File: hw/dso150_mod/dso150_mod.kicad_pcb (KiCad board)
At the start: 4 copper layers, 20.8 x 49.8 mm, 23 parts, among them J1 USB_C_Receptacle_USB2.0, J2 Conn_01x02, J3 Conn_01x02, J4 Conn_01x04, J5 Conn_01x02, J6 Conn_01x01, SW1 SW_SPDT, U1 AP3012, U2 MCP73832-2-OT

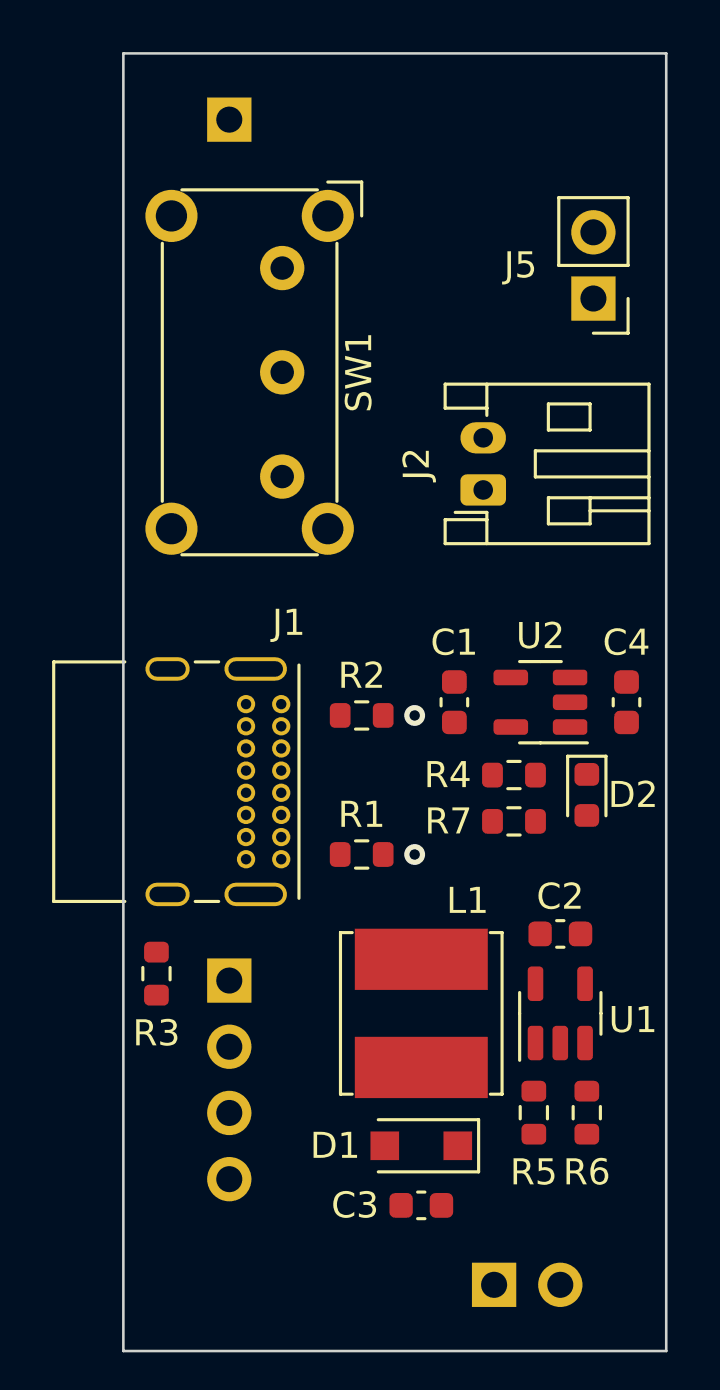
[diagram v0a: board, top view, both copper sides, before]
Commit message: More layout placement, start traces
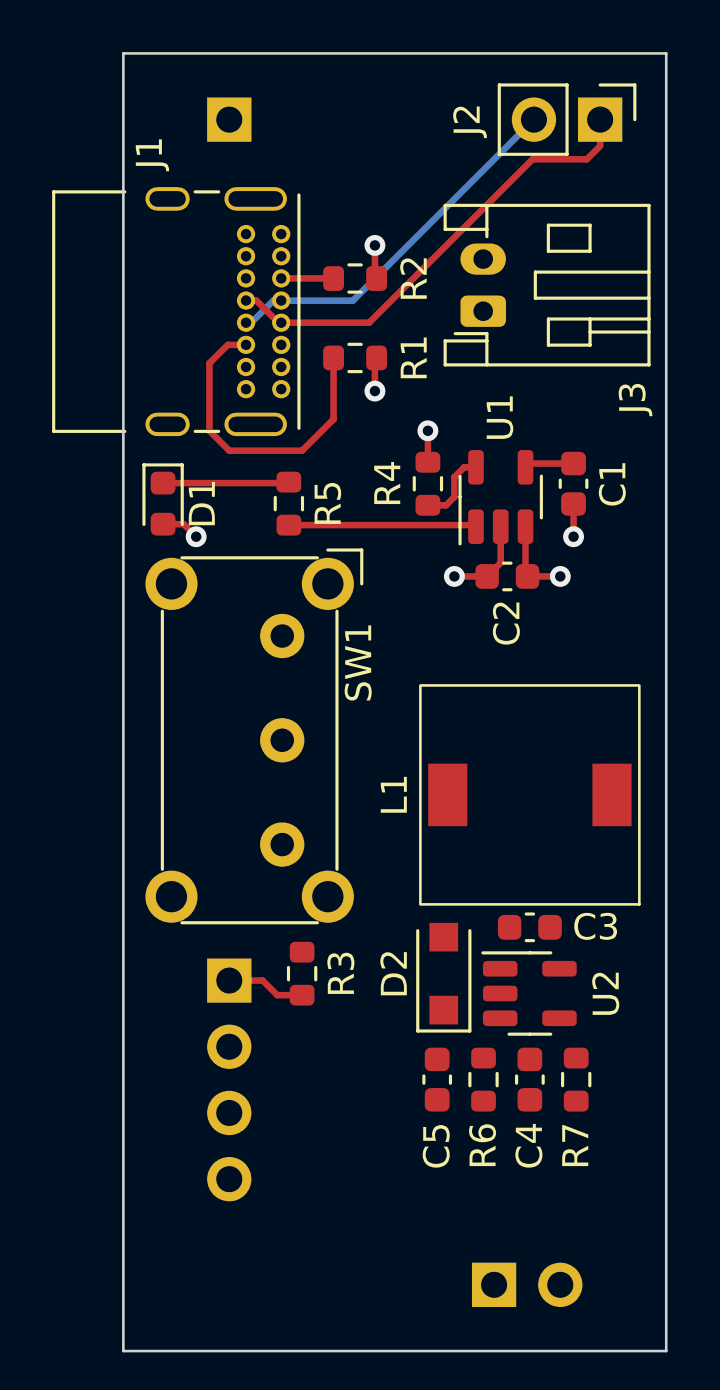
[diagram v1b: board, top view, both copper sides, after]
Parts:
- removed the D1 at (118.6, 124.2)
- removed the U1 at (124.0, 119.1)
- added C4: 4.7p, Capacitor_SMD:C_0603_1608Metric, F.Cu at (122.8, 121.7)
- added D2: MBR1020VL, Diode_SMD:D_SOD-123F, F.Cu at (119.5, 117.6)
- added U2: LMR62014XMF, Package_TO_SOT_SMD:SOT-23-5, F.Cu at (122.8, 118.4)
- C3: renamed from C2; value 1u -> 2.2u
- C5: renamed from C3; value 1u -> 10u
- L1: value 10u -> 12u; footprint Inductor_SMD:L_Bourns_SRN6045TA -> dso150_mod:L_Bourns_SRR0745A
- R6: renamed from R5; value R -> 86.6k
- R7: renamed from R6; value R -> 13.3k
- moved D1 19.7 mm to (108.7, 99.6)
- moved R1 19.1 mm to (116.1, 94.0)
- moved J1 18.0 mm to (113.2, 89.2)
- moved R2 16.8 mm to (116.1, 90.9)
- moved R5 14.9 mm to (113.5, 99.6), turned to 90 degrees
- moved SW1 14.1 mm to (113.3, 104.6)
- moved R4 11.7 mm to (118.9, 98.8), turned to 90 degrees
- moved C1 9.55 mm to (124.5, 98.8)
- moved L1 9.36 mm to (122.8, 110.7), turned to 180 degrees
- moved U1 8.02 mm to (121.7, 99.3), turned to 90 degrees
- moved J2 6.87 mm to (125.5, 84.8), turned to -90 degrees
- moved J3 6.86 mm to (121.0, 92.2)
- moved C2 6.65 mm to (121.9, 102.4), turned to 180 degrees
- moved R3 5.59 mm to (114.0, 117.6)
- moved C5 4.86 mm to (119.2, 121.7), turned to 90 degrees
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- renumbered C4 to C2, D2 to D1, J5 to J2, J2 to J3, J3 to J4, J4 to J5, R7 to R5, U2 to U1
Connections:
- D1 pad 1: Net-(D2-Pad1) -> Net-(R5-Pad2)
- D1 pad 2: Net-(D2-Pad2) (its old number) -> +5V
- J4 pad 1: +9V -> Net-(J4-Pad1)
- R5 pad 1: Net-(D2-Pad2) (its old number) -> Net-(U1-Pad1)
- R5 pad 2: +5V -> Net-(R5-Pad2)
- SW1 pad 1: unconnected-(SW1-Pad1) -> Net-(J4-Pad1)
- SW1 pad 2: unconnected-(SW1-Pad2) -> +9V
- U1 pad 1: Net-(D2-Pad1) -> Net-(U1-Pad1)
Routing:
- net Net-(J1-PadA7): track 0.00 -> 17.8 mm
- net Net-(J1-PadA6): track 0.00 -> 14.3 mm
- net Net-(J1-PadB5): track 0.00 -> 12.2 mm
- net GND: track 0.00 -> 8.44 mm, vias 2 -> 5
- net Net-(U1-Pad1): track 0.00 -> 7.20 mm
- net Net-(R5-Pad2): track 0.00 -> 4.84 mm
- net +5V: track 0.00 -> 3.37 mm, vias 0 -> 1
- net +BATT: track 0.00 -> 3.20 mm, vias 0 -> 1
- net +3.3V: track 0.00 -> 3.03 mm
- net Net-(R4-Pad1): track 0.00 -> 2.89 mm
- net Net-(J1-PadA5): track 0.00 -> 2.01 mm
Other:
- board text added: "JLCJLCJLCJLC"

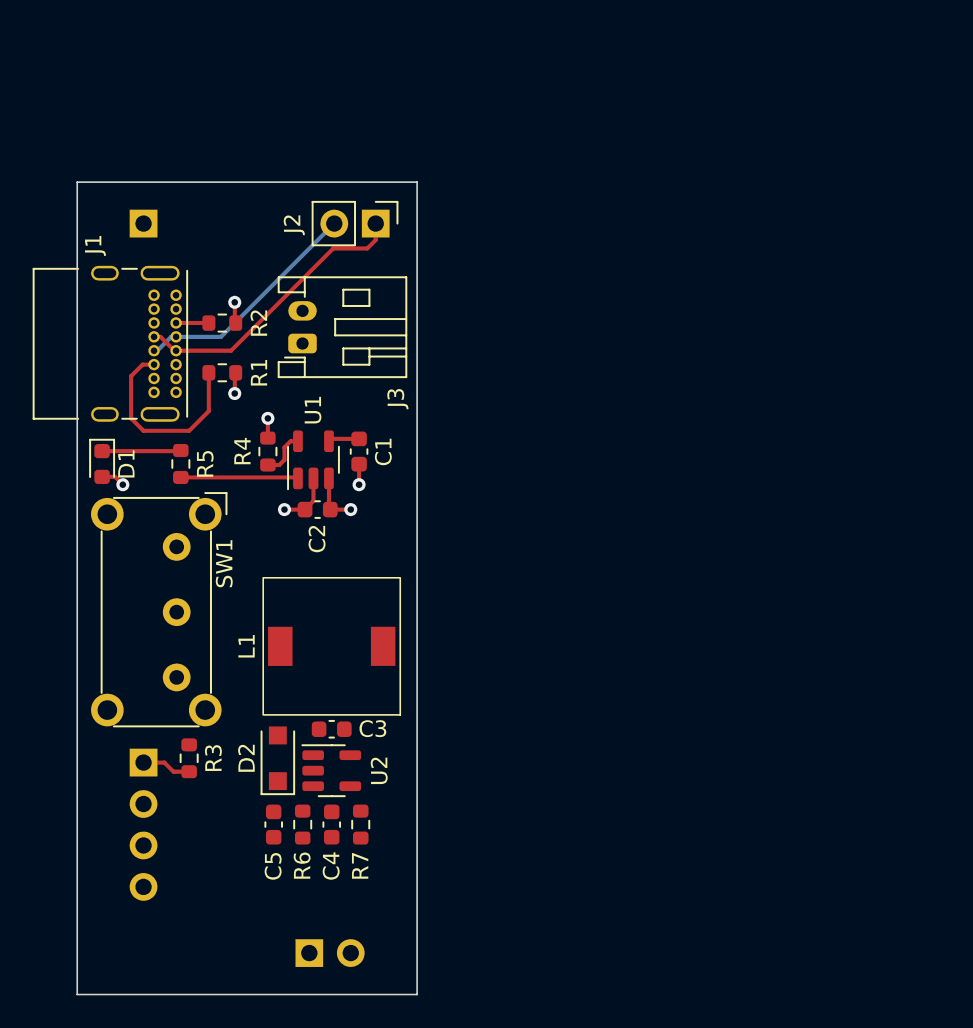
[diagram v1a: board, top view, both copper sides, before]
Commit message: Disable boost converter to conserve battery, first final layout complete
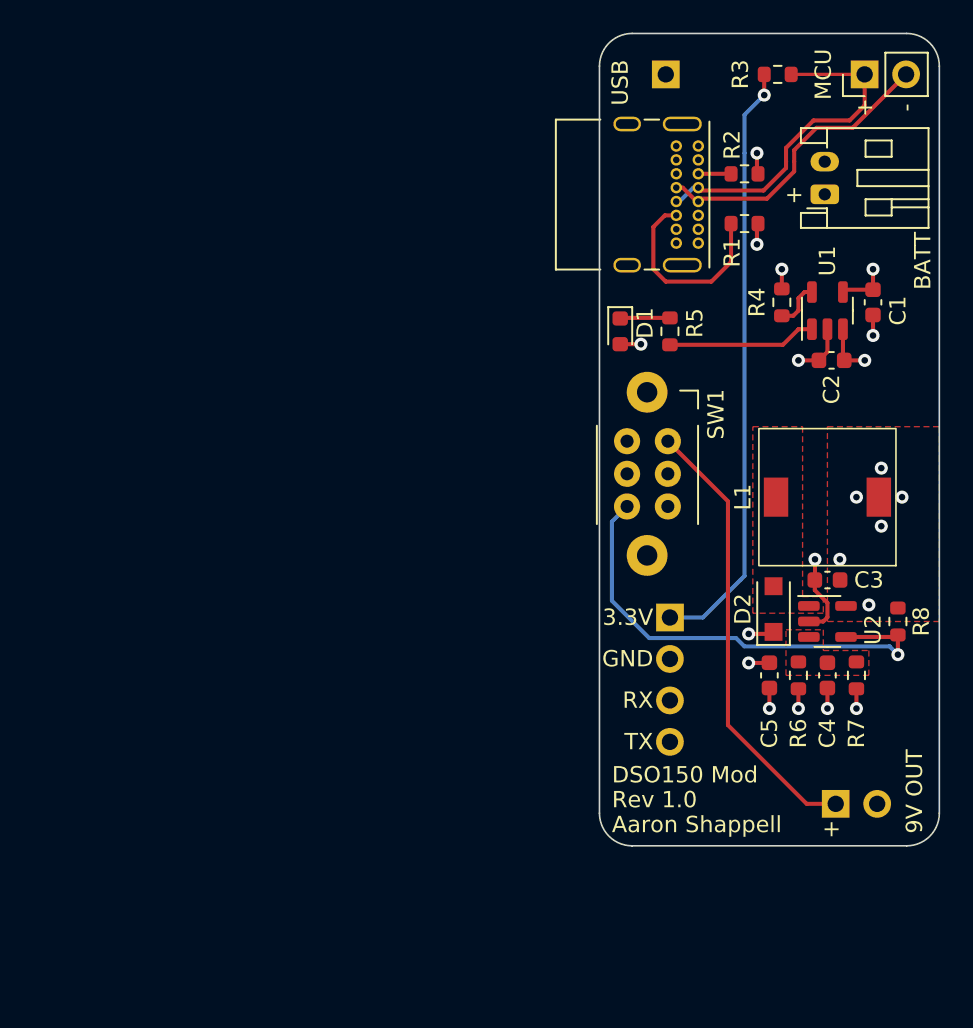
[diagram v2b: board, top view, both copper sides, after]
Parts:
- added R8: 50k, Resistor_SMD:R_0603_1608Metric, F.Cu at (157.5, 109.2)
- J1: footprint Connector_USB:USB_C_Receptacle_GCT_USB4085 -> dso150_mod:USB_C_Receptacle_GCT_USB4085
- SW1: value SW_SPDT -> EG2208; footprint Button_Switch_THT:SW_E-Switch_EG1224_SPDT_Angled -> dso150_mod:SW_E-Switch_EG2208_DPDT_Angled
- moved R3 55.3 mm to (150.1, 75.7), turned to 0 degrees
- moved J4 33.5 mm to (153.7, 120.4)
- moved J5 33.5 mm to (143.5, 109.0)
- moved J6 33.3 mm to (143.3, 75.7)
- moved J1 33.3 mm to (145.2, 80.1)
- moved J3 33.3 mm to (153.0, 83.0)
- moved R1 33.3 mm to (148.1, 84.8)
- moved R2 33.3 mm to (148.1, 81.8)
- moved U1 32.8 mm to (153.2, 90.2)
- moved C1 32.8 mm to (156.0, 89.7)
- moved C2 32.8 mm to (153.4, 93.2)
- moved R4 32.8 mm to (150.4, 89.7)
- moved D1 32.8 mm to (140.5, 91.4)
- moved D2 31.7 mm to (149.9, 108.5)
- moved L1 31.7 mm to (153.2, 101.6)
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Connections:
- J1 pad A6: Net-(J1-PadA6) -> /D+
- J1 pad A7: Net-(J1-PadA7) -> /D-
- J1 pad B6: Net-(J1-PadA6) -> /D+
- J1 pad B7: Net-(J1-PadA7) -> /D-
- J2 pad 1: Net-(J1-PadA7) -> /D+
- J2 pad 2: Net-(J1-PadA6) -> /D-
- R3 pad 2: Net-(J1-PadA6) -> /D+
- U2 pad 4: +BATT -> Net-(R8-Pad2)
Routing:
- net +3.3V: track 3.03 -> 36.9 mm, vias 0 -> 1
- net Net-(R8-Pad2): track 0.00 -> 29.5 mm, vias 0 -> 1
- net Net-(SW1-Pad1): track 0.00 -> 27.5 mm
- net /D+: track 0.00 -> 21.3 mm
- net /D-: track 0.00 -> 18.4 mm
- net Net-(J1-PadA7): track 17.8 -> 0.00 mm
- net Net-(J1-PadA6): track 14.3 -> 0.00 mm
- net GND: track 8.44 -> 16.0 mm, vias 5 -> 8
- net +9V: track 0.00 -> 5.30 mm, vias 0 -> 4
- net Net-(R5-Pad1): track 7.20 -> 9.10 mm
- net Net-(D1-Pad1): track 4.84 -> 3.06 mm
- net +5V: track 3.37 -> 4.43 mm, vias 1 -> 2
- net +BATT: vias 1 -> 7
- added copper zone on In2.Cu, net +5V
- added copper zone on In2.Cu, net +9V
- added copper zone on F.Cu, net +BATT
- added copper zone on In2.Cu, net +BATT
- added copper zone on F.Cu, net Net-(C4-Pad2)
- added copper zone on F.Cu, net Net-(D2-Pad2)
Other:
- outline, holes or cut-outs redrawn
- board text added: "+"
- board text added: "-"
- board text added: "3.3V"
- board text added: "9V OUT"
- board text added: "Aaron Shappell"
- board text added: "BATT"
- board text added: "DSO150 Mod"
- board text added: "GND"
- board text added: "MCU"
- board text added: "RX"
- board text added: "Rev 1.0"
- board text added: "TX"
- board text added: "USB"

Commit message: Add gerbers
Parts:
- C4: value 4.7p -> 470p
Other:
- board text added: "3V3"
- board text removed: "3.3V"
